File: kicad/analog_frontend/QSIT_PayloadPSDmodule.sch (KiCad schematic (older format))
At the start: 60 parts, among them J1 Conn_02x05_Odd_Even, J2 Conn_02x05_Odd_Even, J3 Conn_02x05_Odd_Even, U1 PSDS5990-01, U2 OPA4990IRTER, U3 OPA4990IRTER, U4 OPA4990IRTER, U5 OPA4990IRTER

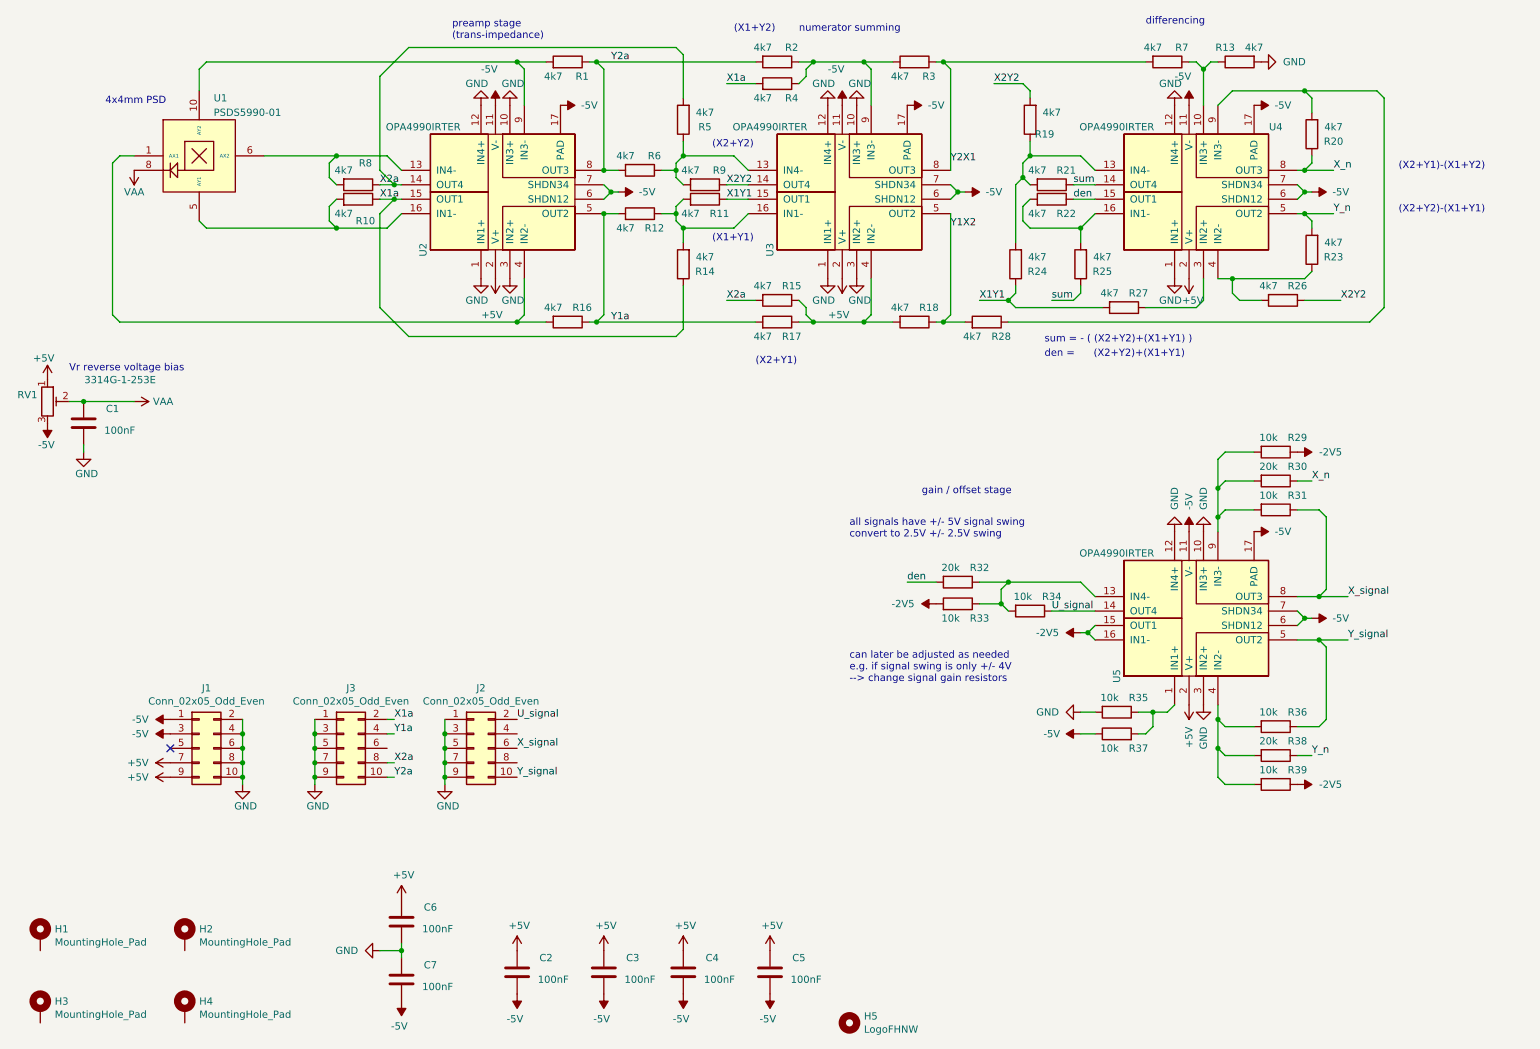
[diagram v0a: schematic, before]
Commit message: added stm32f373cct6
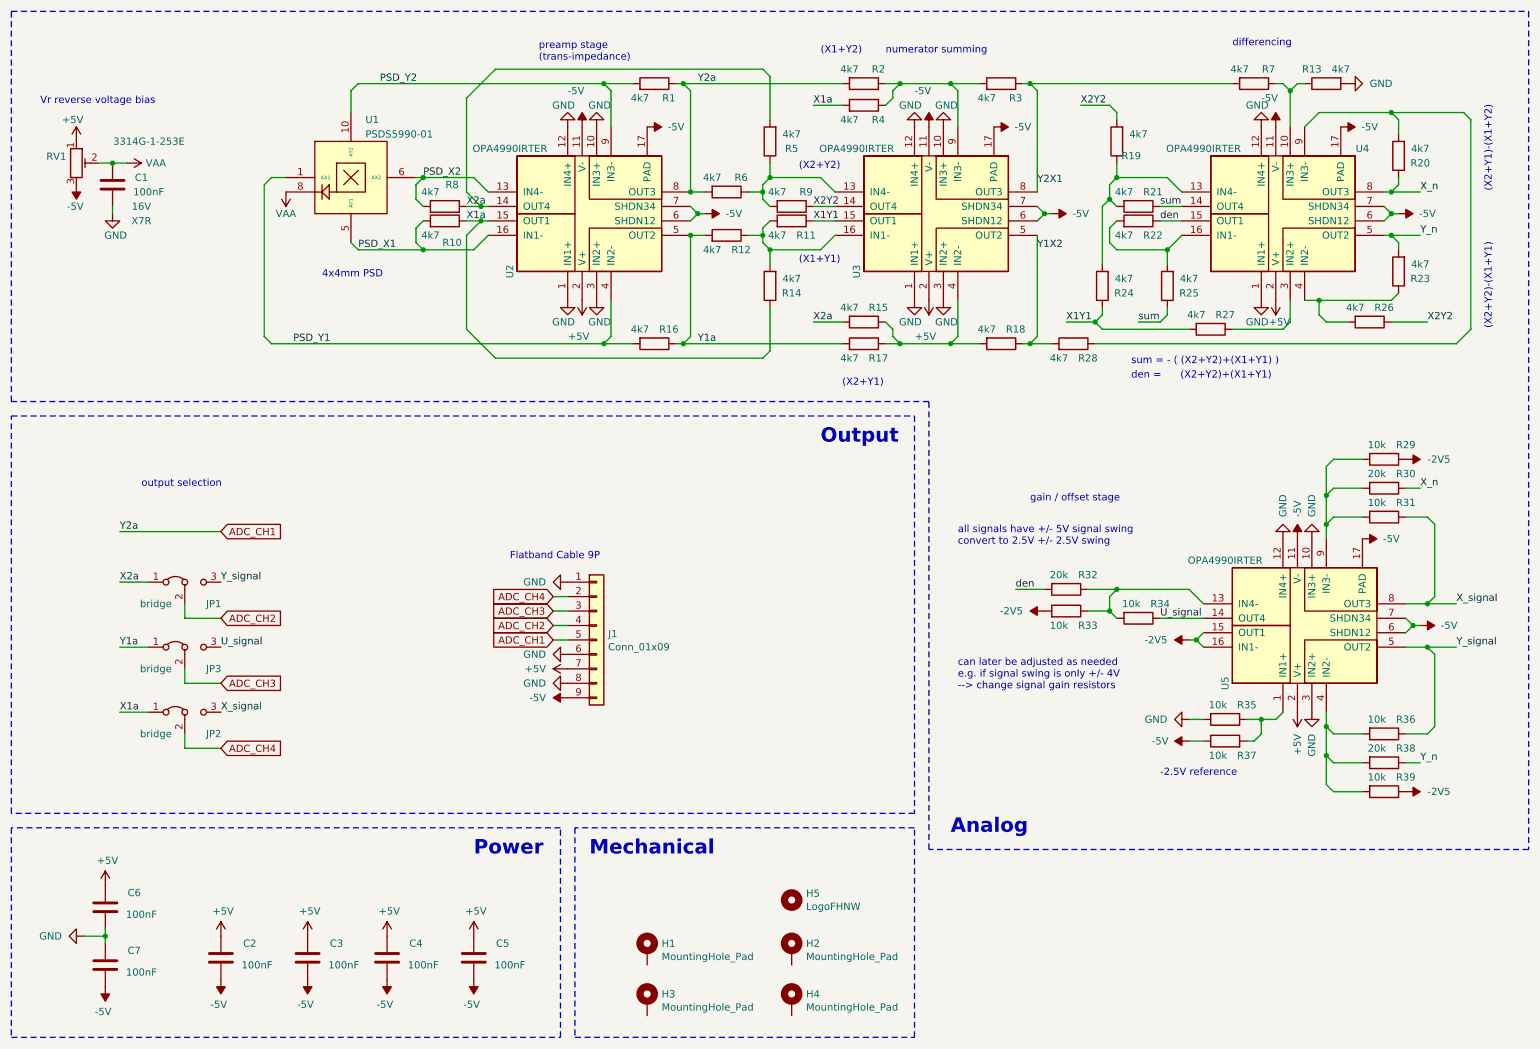
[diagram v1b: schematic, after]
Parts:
- removed J1, J2, J3: Conn_02x05_Odd_Even, Connector_PinHeader_1.27mm:PinHeader_2x05_P1.27mm_Vertical_SMD, symbol Connector_Generic:Conn_02x05_Odd_Even
- added J1: Conn_01x09, Connector_PinHeader_2.54mm:PinHeader_1x09_P2.54mm_Vertical, symbol Connector_Generic:Conn_01x09
- added JP1, JP2, JP3: bridge, Jumper:SolderJumper-3_P1.3mm_Open_RoundedPad1.0x1.5mm, symbol Jumper:Jumper_3_Bridged12
- C1: Type (none) -> X7R; Voltage (none) -> 16V
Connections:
- net +5V: now also J1.7 (Pin_7)
- net -5V: now also J1.9 (Pin_9)
- net GND: now also J1.1 (Pin_1), J1.6 (Pin_6), J1.8 (Pin_8)
- net U_signal: now also JP3.3 (B)
- net X1a: now also JP2.1 (A)
- net X2a: now also JP1.1 (A)
- net X_signal: now also JP2.3 (B)
- net Y1a: now also JP3.1 (A)
- net Y_signal: now also JP1.3 (B)
- net PSD_X2: now reaches R8.2, U1.6 (AX2), U2.13 (IN4-)
- net PSD_X1: now reaches R10.2, U1.5 (AY1), U2.16 (IN1-)
- net PSD_Y1: now reaches R16.2, U1.1 (AX1), U2.4 (‌IN2-)
- net PSD_Y2: now reaches R1.2, U1.10 (AY2), U2.9 (IN3-)
- net Y2a renamed ADC_CH1
- net ADC_CH1: now also J1.5 (Pin_5)
- new net ADC_CH2: J1.4 (Pin_4), JP1.2 (C)
- new net ADC_CH3: J1.3 (Pin_3), JP3.2 (C)
- new net ADC_CH4: J1.2 (Pin_2), JP2.2 (C)
- no-connect marks 1 -> 0
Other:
- note added: "-2.5V reference"
- note added: "Analog"
- note added: "Flatband Cable 9P"
- note added: "Mechanical"
- note added: "Output"
- note added: "Power"
- note added: "output selection"
- moved on the sheet: C1, C2, C3, C4, C5, C6, C7, H1, H2, H3, H4, H5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

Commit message: rev 1 finished - final check on PSD frontend - plotted gerbber for jlc - added simulation for PSD frontend
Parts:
- removed U1: PSDS5990-01, A_Tale_Of_A_Library:HAMAMATSU_PSD_S599001_4mm, symbol A_Tale_Of_A_Library:PSDS5990-01
- removed U2, U3, U4, U5: OPA4990IRTER, Package_DFN_QFN:WQFN-16-1EP_3x3mm_P0.5mm_EP1.6x1.6mm, symbol A_Tale_Of_A_Library:OPA4990IRTER
- added C8: 100nF, Capacitor_SMD:C_0603_1608Metric_Pad1.08x0.95mm_HandSolder, symbol Device:C
- added R40: 4k7, Resistor_SMD:R_0603_1608Metric_Pad0.98x0.95mm_HandSolder, symbol Device:R
- added U1: PSDS5990-01, simonmartin_kicad_lib:HAMAMATSU_PSD_S599001_4mm, symbol simonmartin_kicad_lib:PSDS5990-01
- added U2, U3, U4, U5: OPA4990IRTER, Package_DFN_QFN:WQFN-16-1EP_3x3mm_P0.5mm_EP1.6x1.6mm, symbol simonmartin_kicad_lib:OPA4990IRTER
- C1, C2, C3, C4, C5, C6, C7: footprint Capacitor_SMD:C_0603_1608Metric_Pad1.05x0.95mm_HandSolder -> Capacitor_SMD:C_0603_1608Metric_Pad1.08x0.95mm_HandSolder
- R1, R10, R11, R12, R13, R14, R15, R16, R17, R18, R19, R2, R20, R21, R22, R23, R24, R25, R26, R27, R28, R29, R3, R30, R31, R32, R33, R34, R35, R36, R37, R38, R39, R4, R5, R6, R7, R8, R9: footprint Resistor_SMD:R_0603_1608Metric_Pad1.05x0.95mm_HandSolder -> Resistor_SMD:R_0603_1608Metric_Pad0.98x0.95mm_HandSolder
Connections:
- net +5V: now also U2.2 (V+), U3.2 (V+), U4.2 (V+), U5.2 (V+)
- net -2V5: now also U5.15 (OUT1), U5.16 (IN1-)
- net -5V: now also U2.11 (V-), U2.17 (PAD), U2.6 (SHDN12), U2.7 (SHDN34), U3.11 (V-), U3.17 (PAD), U3.6 (SHDN12), U3.7 (SHDN34), U4.11 (V-), U4.17 (PAD), U4.6 (SHDN12), U4.7 (SHDN34), U5.11 (V-), U5.17 (PAD), U5.6 (SHDN12), U5.7 (SHDN34)
- net ADC_CH1: now also U2.8 (OUT3)
- net GND: now also C8.1, R40.2, U2.1 (IN1+), U2.10 (IN3+), U2.12 (IN4+), U2.3 (IN2+), U3.1 (IN1+), U3.10 (IN3+), U3.12 (IN4+), U3.3 (IN2+), U4.1 (IN1+), U4.12 (IN4+), U5.10 (IN3+), U5.12 (IN4+), U5.3 (IN2+)
- net PSD_X1: now also U1.5 (AY1), U2.16 (IN1-)
- net PSD_X2: now also U1.6 (AX2), U2.13 (IN4-)
- net PSD_Y1: now also U1.1 (AX1), U2.4 (‌IN2-)
- net PSD_Y2: now also U1.10 (AY2), U2.9 (IN3-)
- net U_signal: now also U5.14 (OUT4)
- net VAA: now also U1.8
- net X1Y1: now also U3.15 (OUT1)
- net X1a: now also U2.15 (OUT1)
- net X2Y2: now also U3.14 (OUT4)
- net X2a: now also U2.14 (OUT4)
- net X_n: now also U4.8 (OUT3)
- net X_signal: now also U5.8 (OUT3)
- net Y1X2: now also U3.5 (OUT2)
- net Y1a: now also U2.5 (OUT2)
- net Y2X1: now also U3.8 (OUT3)
- net Y_n: now also U4.5 (OUT2)
- net Y_signal: now also U5.5 (OUT2)
- net den: now also U4.15 (OUT1)
- net sum: now also U4.14 (OUT4)
- net at R5.1, R6.1, R9.2: now also U3.13 (IN4-)
- net at R11.2, R12.1, R14.2: now also U3.16 (IN1-)
- net at R15.1, R17.1, R18.2: now also U3.4 (‌IN2-)
- net at R2.1, R3.2, R4.1: now also U3.9 (IN3-)
- net at R35.1, R37.2: now also C8.2, U5.1 (IN1+)
- net at R13.1, R7.1: now also U4.10 (IN3+)
- net at R19.1, R21.2, R24.2: now also U4.13 (IN4-)
- net at R22.2, R25.2: now also U4.16 (IN1-)
- net at R27.1: now also R40.1, U4.3 (IN2+)
- net at R23.1, R26.2: now also U4.4 (‌IN2-)
- net at R20.2, R28.1: now also U4.9 (IN3-)
- net at R32.1, R33.1, R34.2: now also U5.13 (IN4-)
- net at R36.2, R38.2, R39.2: now also U5.4 (‌IN2-)
- net at R29.2, R30.2, R31.2: now also U5.9 (IN3-)
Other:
- note added: "- use precision resistors\n- calibrate the DSP"
- note added: "these signals do not make sense\nto directly go to the ADC because they \nmay have negative output swing"
- moved on the sheet: R26, R35, R37

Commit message: fixed wrong connection to PSD X/Y axis
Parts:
- R29, R33, R39: value 10k -> 20k
- R30, R32, R38: value 20k -> 40k
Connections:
- net PSD_X1: now also U1.1 (AX1); no longer U1.5 (AY1)
- net PSD_Y1: now also U1.5 (AY1); no longer U1.1 (AX1)
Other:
- note added: "all signals have +/- 5V signal swing\nconvert to 1.25V +/- 1.25V swing"
- note removed: "all signals have +/- 5V signal swing\nconvert to 2.5V +/- 2.5V swing"
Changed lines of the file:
@@
 Wire Wire Line
 	3800 2250 3450 2250
-Wire Wire Line
-	3000 2250 2950 2200
 $Comp
 L Device:R R10
@@
 	4750 2850 4700 2900
 Wire Wire Line
-	2400 2900 2350 2850
-Wire Wire Line
 	4750 2600 4750 2850
-Wire Wire Line
-	2350 1800 2350 2850
 Wire Wire Line
 	4700 2900 4900 2900
@@
 P 10100 3900
 F 0 "R30" V 10000 4050 50  0000 C CNN
-F 1 "20k" V 10000 3850 50  0000 C CNN
+F 1 "40k" V 10000 3850 50  0000 C CNN
 F 2 "Resistor_SMD:R_0603_1608Metric_Pad0.98x0.95mm_HandSolder" V 10030 3900 50  0001 C CNN
 F 3 "~" H 10100 3900 50  0001 C CNN
@@
 P 10100 5800
 F 0 "R38" V 10000 5950 50  0000 C CNN
-F 1 "20k" V 10000 5750 50  0000 C CNN
+F 1 "40k" V 10000 5750 50  0000 C CNN
 F 2 "Resistor_SMD:R_0603_1608Metric_Pad0.98x0.95mm_HandSolder" V 10030 5800 50  0001 C CNN
 F 3 "~" H 10100 5800 50  0001 C CNN
@@
 P 7900 4600
 F 0 "R32" V 7800 4750 50  0000 C CNN
-F 1 "20k" V 7800 4550 50  0000 C CNN
+F 1 "40k" V 7800 4550 50  0000 C CNN
 F 2 "Resistor_SMD:R_0603_1608Metric_Pad0.98x0.95mm_HandSolder" V 7830 4600 50  0001 C CNN
 F 3 "~" H 7900 4600 50  0001 C CNN
@@
 P 7900 4750
 F 0 "R33" V 7800 4900 50  0000 C CNN
-F 1 "10k" V 7800 4700 50  0000 C CNN
+F 1 "20k" V 7800 4700 50  0000 C CNN
 F 2 "Resistor_SMD:R_0603_1608Metric_Pad0.98x0.95mm_HandSolder" V 7830 4750 50  0001 C CNN
 F 3 "~" H 7900 4750 50  0001 C CNN
@@
 P 10100 3700
 F 0 "R29" V 10000 3850 50  0000 C CNN
-F 1 "10k" V 10000 3650 50  0000 C CNN
+F 1 "20k" V 10000 3650 50  0000 C CNN
 F 2 "Resistor_SMD:R_0603_1608Metric_Pad0.98x0.95mm_HandSolder" V 10030 3700 50  0001 C CNN
 F 3 "~" H 10100 3700 50  0001 C CNN
@@
 P 10100 6000
 F 0 "R39" V 10000 6150 50  0000 C CNN
-F 1 "10k" V 10000 5950 50  0000 C CNN
+F 1 "20k" V 10000 5950 50  0000 C CNN
 F 2 "Resistor_SMD:R_0603_1608Metric_Pad0.98x0.95mm_HandSolder" V 10030 6000 50  0001 C CNN
 F 3 "~" H 10100 6000 50  0001 C CNN
@@
 Text Label 1350 4550 0    50   ~ 0
 X2a
-Text Notes 2750 2450 0    50   ~ 0
+Text Notes 2350 1450 0    50   ~ 0
 4x4mm PSD
 Text Notes 4250 950  0    50   ~ 10
@@
 gain / offset stage
 Text Notes 7050 4100 0    50   ~ 0
-all signals have +/- 5V signal swing\nconvert to 2.5V +/- 2.5V swing
+all signals have +/- 5V signal swing\nconvert to 1.25V +/- 1.25V swing
 Text Notes 7250 4400 0    50   ~ 0
 can later be adjusted as needed\ne.g. if signal swing is only +/- 4V\n--> change signal gain resistors
@@
 	3400 1750 3450 1750
 Connection ~ 3450 1750
-Wire Wire Line
-	3000 2250 3450 2250
 Connection ~ 3450 2250
-Wire Wire Line
-	2400 2900 4700 2900
-Connection ~ 4700 2900
 Wire Wire Line
 	4700 1100 3000 1100
@@
 	1400 1650 1300 1650
 Connection ~ 1300 1650
-Text Label 2550 2900 0    50   ~ 0
+Text Label 3050 2900 0    50   ~ 0
 PSD_Y1
 Text Label 3150 1100 0    50   ~ 0
 PSD_Y2
-Text Label 3000 2250 0    50   ~ 0
+Text Label 2450 2250 0    50   ~ 0
 PSD_X1
 Text Label 3450 1750 0    50   ~ 0
@@
 	0    -1   -1   0
 $EndComp
-$Comp
-L simonmartin_kicad_lib:PSDS5990-01 U1
-U 1 1 61BA2C29
-P 2950 1750
-F 0 "U1" H 3050 2150 50  0000 L CNN
-F 1 "PSDS5990-01" H 3000 2050 50  0000 L CNN
-F 2 "simonmartin_kicad_lib:HAMAMATSU_PSD_S599001_4mm" H 2400 2050 50  0001 C CNN
-F 3 "" H 5050 1550 50  0001 C CNN
-	1    2950 1750
-	1    0    0    -1
-$EndComp
 Text Notes 1200 5650 1    50   ~ 0
 these signals do not make sense\nto directly go to the ADC because they \nmay have negative output swing
@@
 	9250 5850 9250 5600
 Connection ~ 9250 5600
+$Comp
+L simonmartin_kicad_lib:PSDS5990-01 U1
+U 1 1 61BA2C29
+P 2950 1750
+F 0 "U1" H 3050 2150 50  0000 L CNN
+F 1 "PSDS5990-01" H 3000 2050 50  0000 L CNN
+F 2 "simonmartin_kicad_lib:HAMAMATSU_PSD_S599001_4mm" H 2400 2050 50  0001 C CNN
+F 3 "" H 5050 1550 50  0001 C CNN
+	1    2950 1750
+	1    0    0    -1
+$EndComp
+Wire Wire Line
+	4700 2900 3000 2900
+Wire Wire Line
+	3000 2900 2950 2850
+Wire Wire Line
+	2950 2850 2950 2200
+Connection ~ 4700 2900
+Wire Wire Line
+	2400 2250 2350 2200
+Wire Wire Line
+	2350 2200 2350 1800
+Wire Wire Line
+	2400 2250 3450 2250
 $EndSCHEMATC
